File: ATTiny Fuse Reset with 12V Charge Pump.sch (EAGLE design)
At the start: 21 parts, among them U2 ARDUINOR3-BPLACE, U3 ATTINY85-20PU

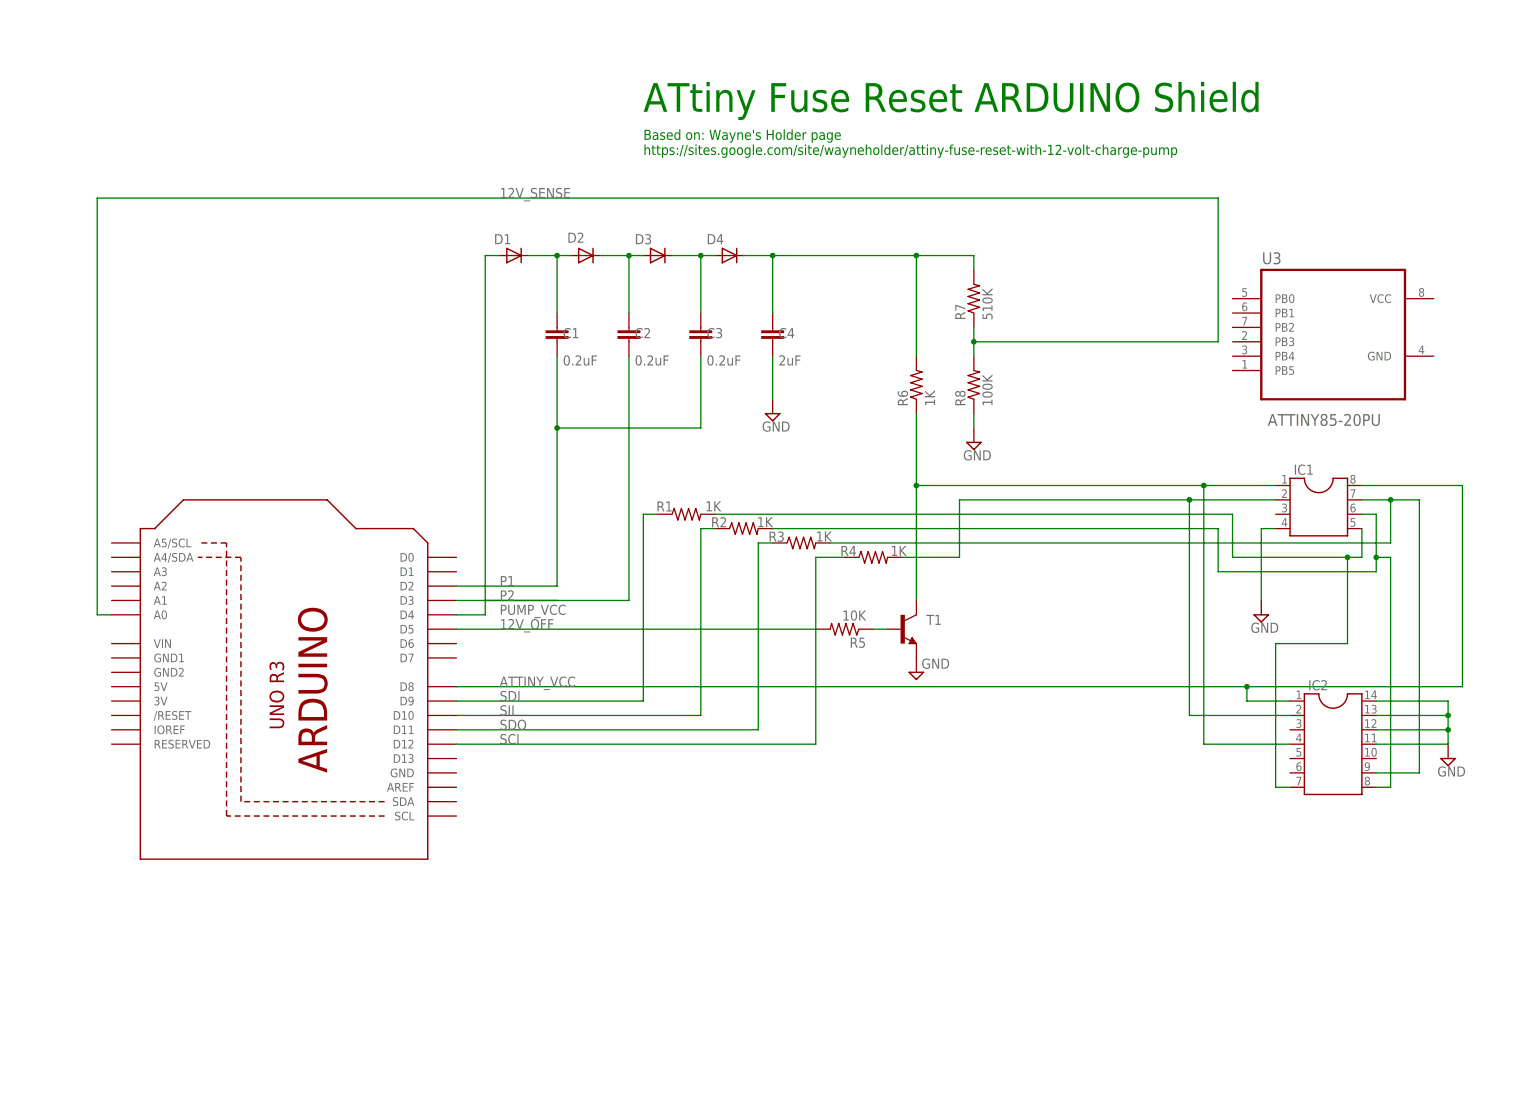
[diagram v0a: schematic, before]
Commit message: need to add ISP header
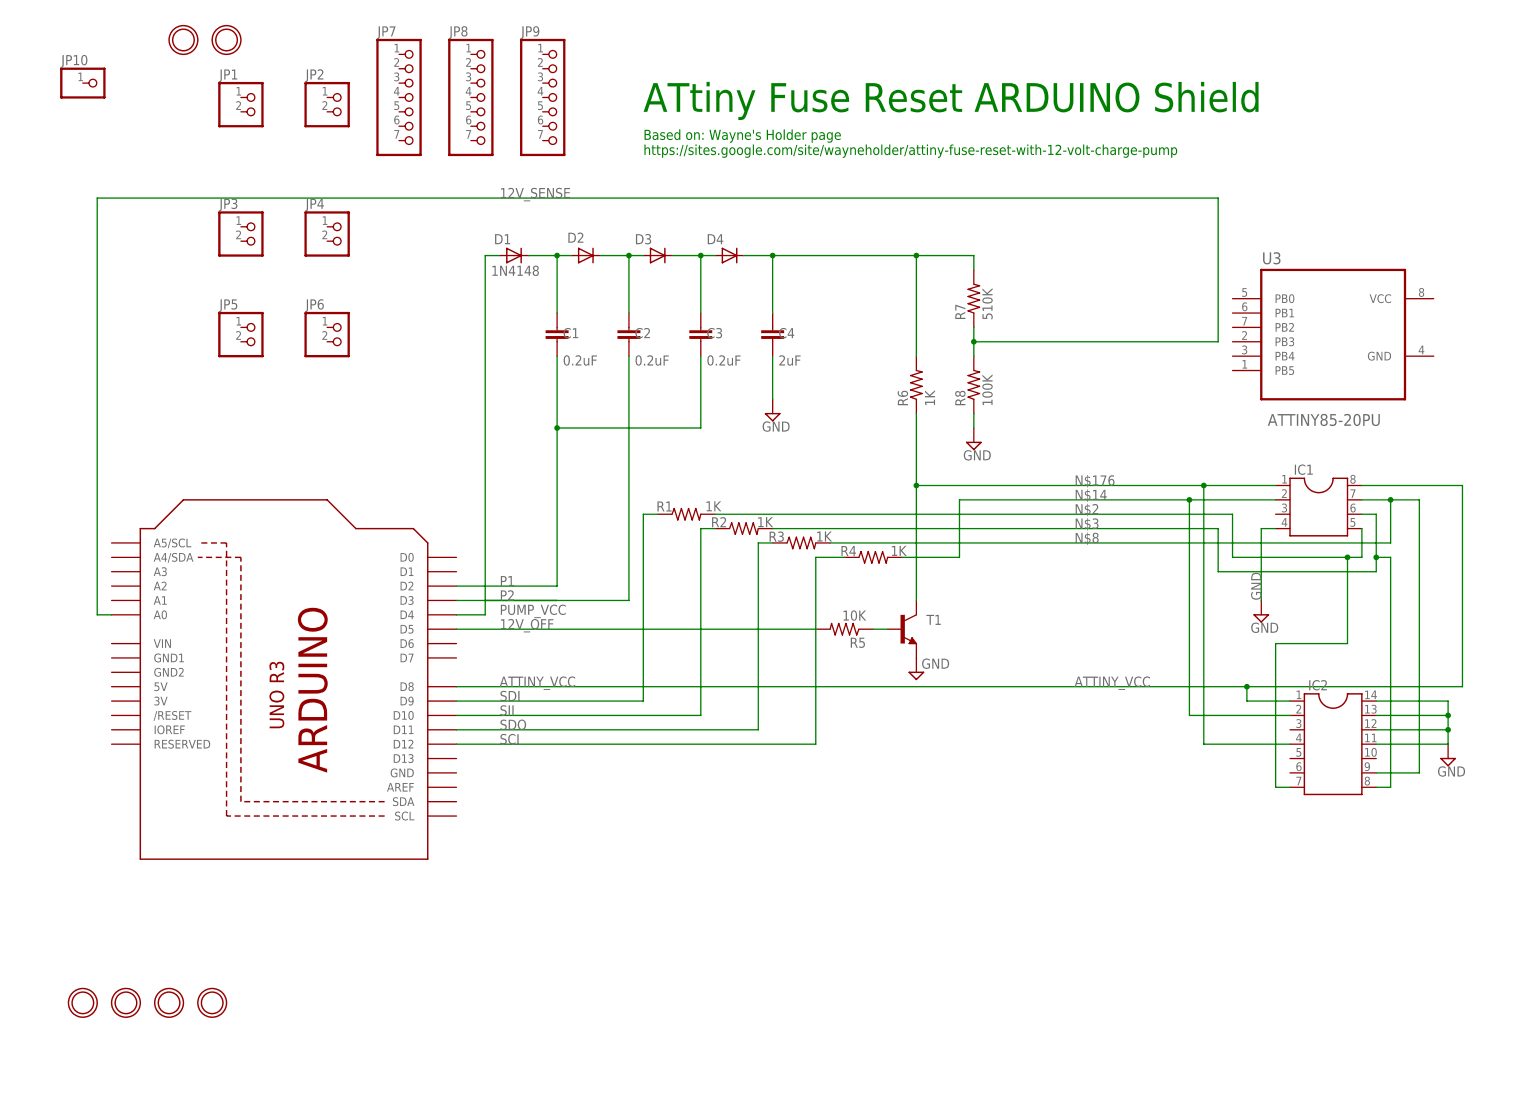
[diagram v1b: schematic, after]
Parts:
- added JP1, JP2, JP3, JP4, JP5, JP6: (no value), ATtami:HEADER-1X2ROUND
- added JP10: (no value), ATtami:PINHD-1X1
- added JP7, JP8, JP9: (no value), ATtami:HEADER-1X7ROUND
- added U$1, U$2, U$3, U$4, U$5, U$6: MOUNTINGHOLE2.0, ATtami:MOUNTINGHOLE2.0
- D1: value (none) -> 1N4148
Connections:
- removed net N$13: D1.A
- removed net N$5: IC1.2, IC2.2, R4.2
- net N$14: now also IC1.2, IC2.2, R4.2
- net PUMP_VCC: now also D1.A

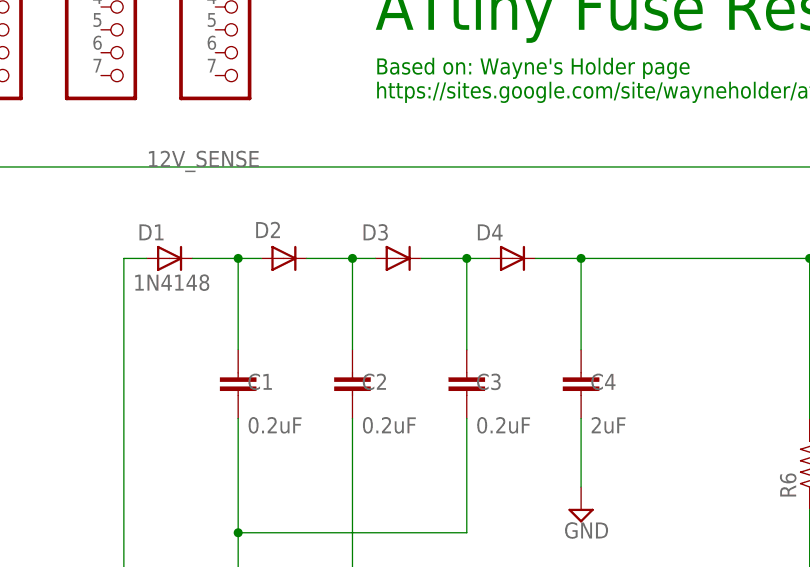
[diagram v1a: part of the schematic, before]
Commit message: added 1N4148 value
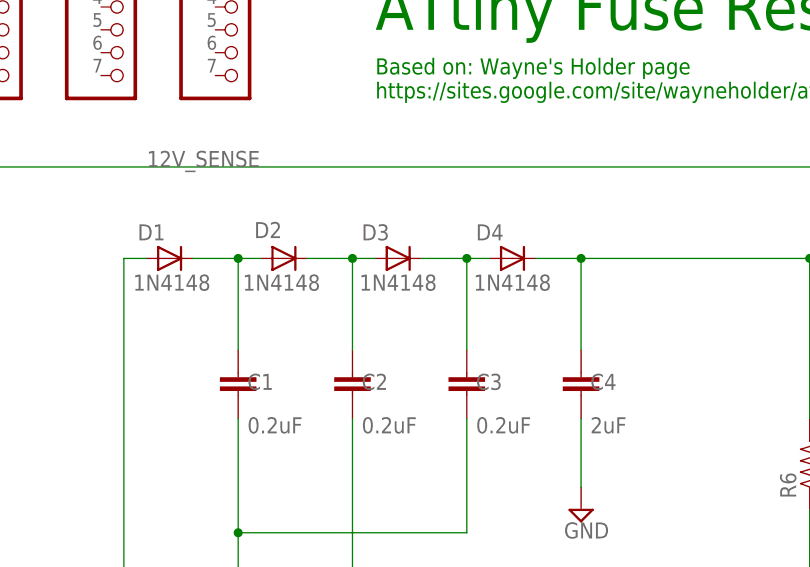
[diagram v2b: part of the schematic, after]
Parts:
- D2, D3, D4: value (none) -> 1N4148
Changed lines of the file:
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@@
 <part name="R8" library="ATtami" deviceset="RESISTOR" device="0805-RES" value="100K"/>
 <part name="D1" library="ATtami" deviceset="SCHOTTKY-DIODE" device="SOD-323" value="1N4148"/>
-<part name="D2" library="ATtami" deviceset="SCHOTTKY-DIODE" device="SOD-323"/>
-<part name="D3" library="ATtami" deviceset="SCHOTTKY-DIODE" device="SOD-323"/>
-<part name="D4" library="ATtami" deviceset="SCHOTTKY-DIODE" device="SOD-323"/>
+<part name="D2" library="ATtami" deviceset="SCHOTTKY-DIODE" device="SOD-323" value="1N4148"/>
+<part name="D3" library="ATtami" deviceset="SCHOTTKY-DIODE" device="SOD-323" value="1N4148"/>
+<part name="D4" library="ATtami" deviceset="SCHOTTKY-DIODE" device="SOD-323" value="1N4148"/>
 <part name="T1" library="dp_devices" deviceset="TRANSISTOR_BJT_NPN" device="-SOT-23-BCE"/>
 <part name="C1" library="ATtami" deviceset="CAP" device="0805" value="0.2uF"/>

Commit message: some caretaking
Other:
- moved on the sheet: JP1, JP2, JP3, JP4, JP9
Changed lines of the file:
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@@
 <instance part="IC2" gate="G$1" x="-88.9" y="50.8"/>
 <instance part="SUPPLY2" gate="GND" x="-68.58" y="48.26"/>
-<instance part="JP1" gate="G$1" x="-279.4" y="162.56"/>
-<instance part="JP2" gate="G$1" x="-264.16" y="162.56"/>
-<instance part="JP3" gate="G$1" x="-279.4" y="139.7"/>
-<instance part="JP4" gate="G$1" x="-264.16" y="139.7"/>
+<instance part="JP1" gate="G$1" x="-279.4" y="109.22"/>
+<instance part="JP2" gate="G$1" x="-264.16" y="109.22"/>
+<instance part="JP3" gate="G$1" x="-292.1" y="162.56"/>
+<instance part="JP4" gate="G$1" x="-281.94" y="162.56"/>
 <instance part="JP5" gate="G$1" x="-279.4" y="121.92"/>
 <instance part="JP6" gate="G$1" x="-264.16" y="121.92"/>
 <instance part="JP7" gate="A" x="-251.46" y="165.1"/>
 <instance part="JP8" gate="A" x="-238.76" y="165.1"/>
-<instance part="JP9" gate="A" x="-226.06" y="165.1"/>
+<instance part="JP9" gate="A" x="-271.78" y="165.1"/>
 <instance part="U$1" gate="G$1" x="-292.1" y="175.26"/>
 <instance part="U$2" gate="G$1" x="-284.48" y="175.26"/>

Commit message: started library of parts
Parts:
- removed U3: ATTINY85-20PU, Atmel_By_element14_Batch_1-00:ATTINY85-20SU
- added C5: 0.2uF, ATtami:CAP0805
- added D5: 1N4148, ATtami:SCHOTTKY-DIODESOD-323
- added JP11: (no value), SparkFun-Connectors:M03X2
- added JP12: (no value), microbuilder:HEADER-2X5
- added LED1: (no value), ATtami:LED-0805
- added R10: 10k, ATtami:RESISTOR0805-RES
- added R9: 1K, ATtami:RESISTOR0805-RES
- added U$7: SWITCH_SPDT, SparkFun-Electromechanical:SWITCH_SPDT
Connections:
- removed net N$176: IC1.1, IC2.4, R6.1, T1.C
- new net N$4: LED1.C, R9.1
- new net N$5: D5.A, R10.2
- new net N$6: C5.1, U2./RESET
- new net N$7: C5.2, U$7.O
- new net N$9: U$7.S, U2.D6
- new net PB5: D5.C, IC1.1, IC2.4, JP11.5, JP12.5, R6.1, T1.C
- new net VCC: JP11.2, JP12.2
- net ATTINY_VCC: now also LED1.A, R10.1
- net GND: now also JP11.6, JP12.10, JP12.4, JP12.6, JP12.8, R9.2, U$7.P
- net SDI: now also JP11.4, JP12.1
- net SDO: now also JP11.3, JP12.7
- net SII: now also JP11.1, JP12.9
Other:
- note added: "1 5 6 7 4 8"
- note added: "10 11 12 13"
- note added: "4 7 8 9 14 1"
- note added: "FUNC | ARD | ATTINY85 | ATTINY84 slave/rst | mosi | miso | sck | gnd | vcc |"
- note added: "fuse sense"
- note added: "miso"
- note added: "mosi"
- note added: "reset"
- note added: "sck"
- moved on the sheet: JP1, JP2, JP5, JP6

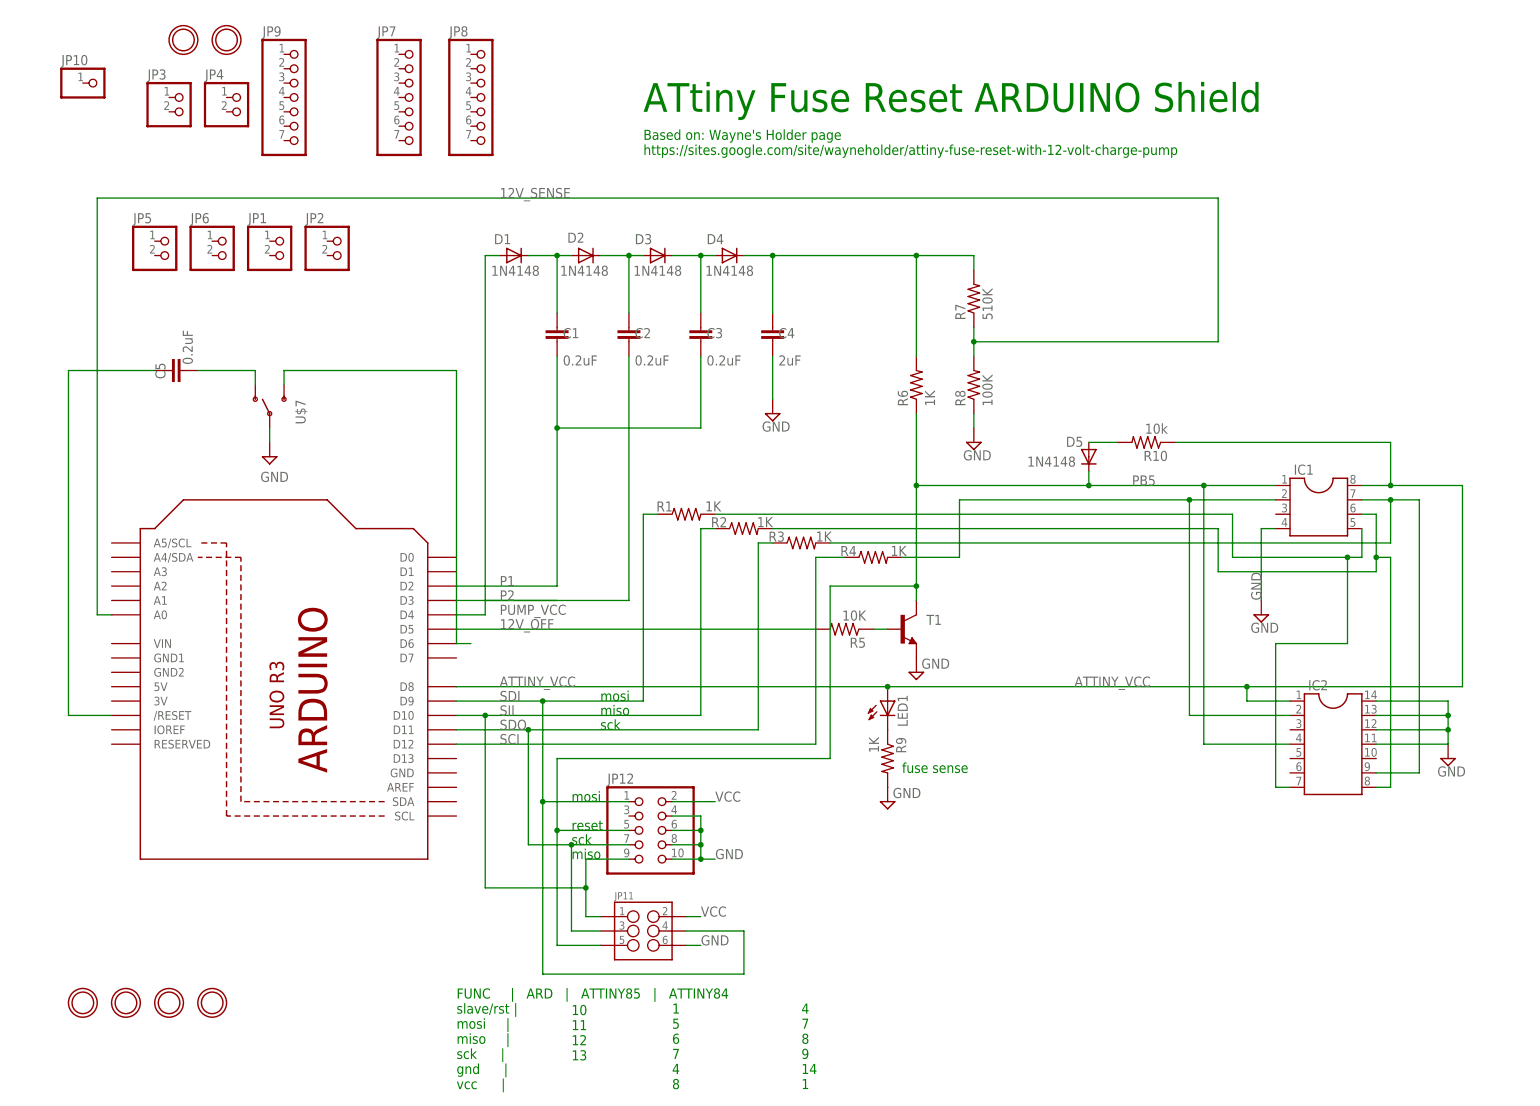
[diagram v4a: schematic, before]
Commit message: Added 12V protecting Zener
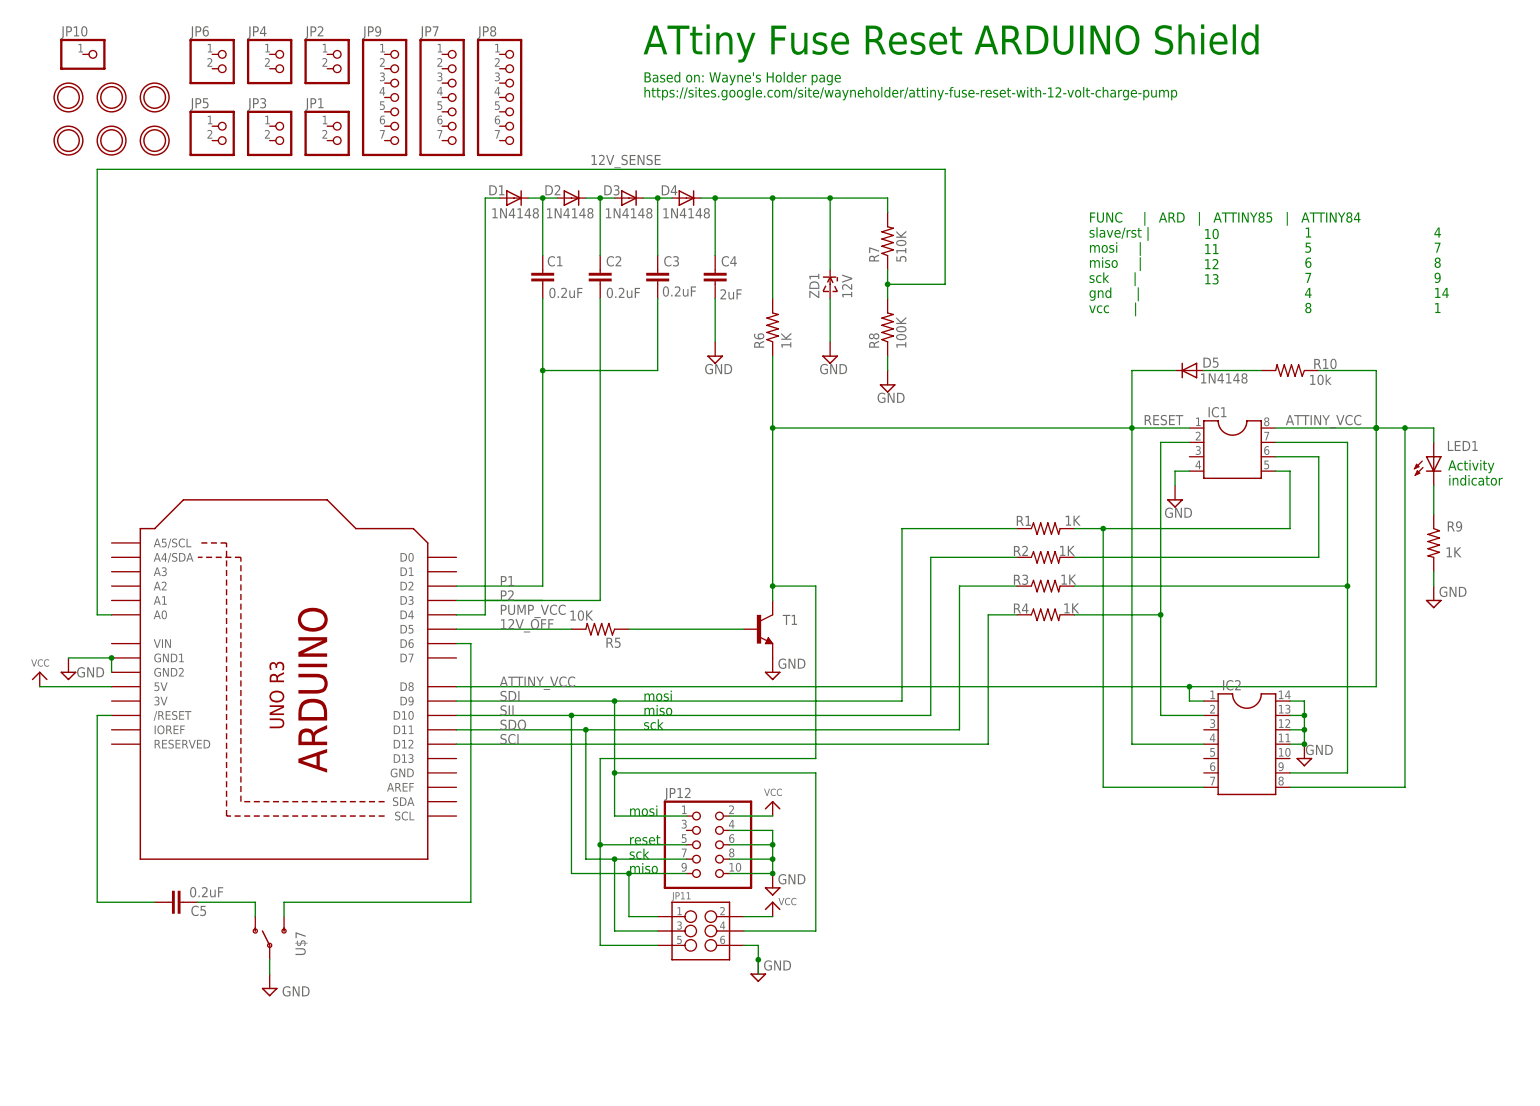
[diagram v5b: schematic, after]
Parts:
- added ZD1: 12V, dp_devices:ZENERSOD-123
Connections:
- net PB5 renamed RESET
- removed net N$1: IC2.11, IC2.12, IC2.13, IC2.14
- removed net N$3: IC1.6, IC2.8, R2.2
- new net N$13: IC1.6, R2.2
- net ATTINY_VCC: now also IC2.8
- net GND: now also IC2.11, IC2.12, IC2.13, IC2.14, U2.GND1, U2.GND2, ZD1.A
- net N$14: now also ZD1.C
- net VCC: now also U2.5V
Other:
- note added: "Activity indicator"
- note removed: "fuse sense"
- moved on the sheet: C1, C2, C3, C4, C5, D1, D2, D3, D4, D5, IC1, IC2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

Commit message: Some cosmetic changes
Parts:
- C5: value 0.2uF -> 10uF
- ZD1: value 12V -> 12V_zener
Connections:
- net RESET renamed HV/RESET
- new net 12V: C4.1, D4.C, R6.2, R7.2, ZD1.C
- net N$14: no longer C4.1, D4.C, R6.2, R7.2, ZD1.C
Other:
- moved on the sheet: C1, C2, C3, C4, C5, D1, D2, D3, D4, IC2, JP11, JP12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
